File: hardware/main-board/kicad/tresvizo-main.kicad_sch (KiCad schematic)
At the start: 0 parts

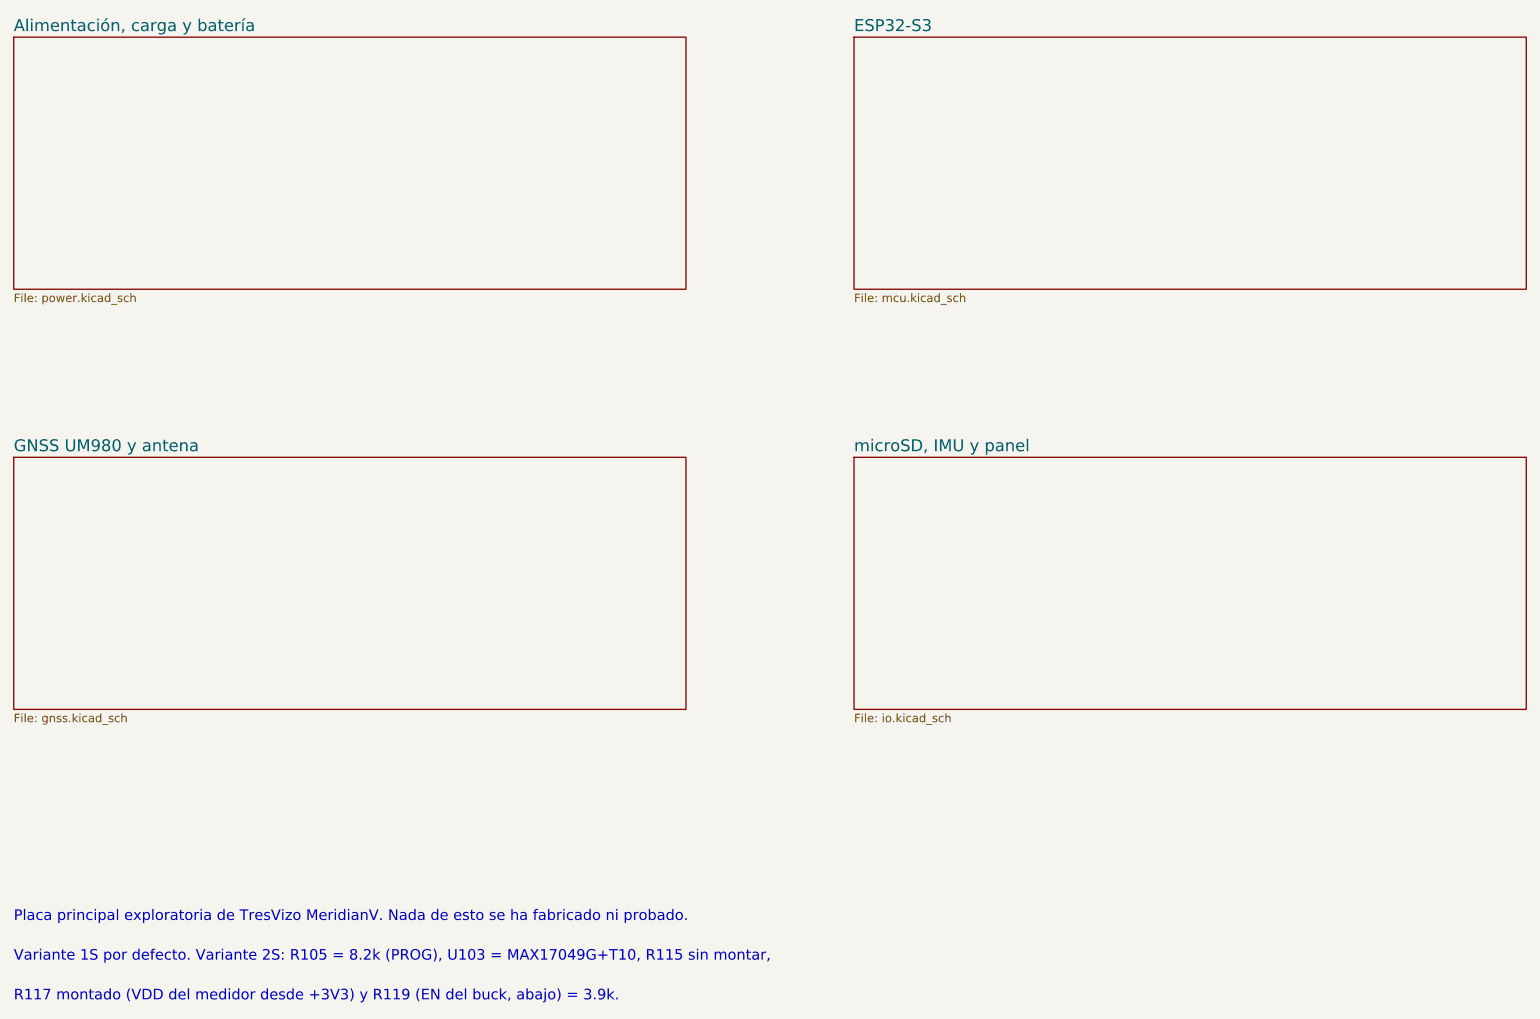
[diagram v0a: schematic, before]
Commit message: Placa principal v0.2: UM980 y BMI088 por cable, conectores hacia cantos o zonas libres, placa panel-usb y un solo panel para JLCPCB
- 46 x 64 mm, 4 capas. El UM980 queda en su carrier BDLX por J301 (GH 8) con 5 V conmutable
  (TPS63070, GPIO45) y el BMI088 vuelve a la tapa por I2C en un segundo bus (J405, GH 7).
- Todos los conectores de cable son GH o SH de 8 pines o menos (kit del propietario), salvo la
  batería (PH 2). Cada uno apunta a un canto o a una zona libre con sitio para la clavija
  enchufada y su cable: áreas de regla clavija_* en el DRC y kicad/plugs.json para el CAD.
- La placa sube 2.5 mm en el tubo (z 23.5-87.5) para que las clavijas del canto inferior tengan
  7.6 mm hasta la base; rieles propuestos en z 39-90 y agujeros nuevos. Comprobada en FreeCAD
  contra V2.2 con modelos 3D y clavijas: sin choques.
- Cargador según el ejemplo de TI: bootstrap junto a sus pines (0.9 y 1.6 mm), salida en abanico
  de la fila inferior y potencia solo por capas externas.
- Placa panel-usb (USB-C a ras de la tapa del panel, GH 8 a J101) y panel de las dos placas con un
  BOM y un CPL (panelize.py, 82.8 x 78 mm).
- Serigrafía sin solapes (silk_clean.py) y logotipo de TresVizo con www.tresvizo.com.
- ERC 0; DRC con 0 errores, 0 avisos, 0 sin conectar y 0 diferencias de paridad en las dos
  placas y el panel. Costo estimado de montaje y piezas: 211 USD por 5 juegos en un panel, sin
  el PCB desnudo.
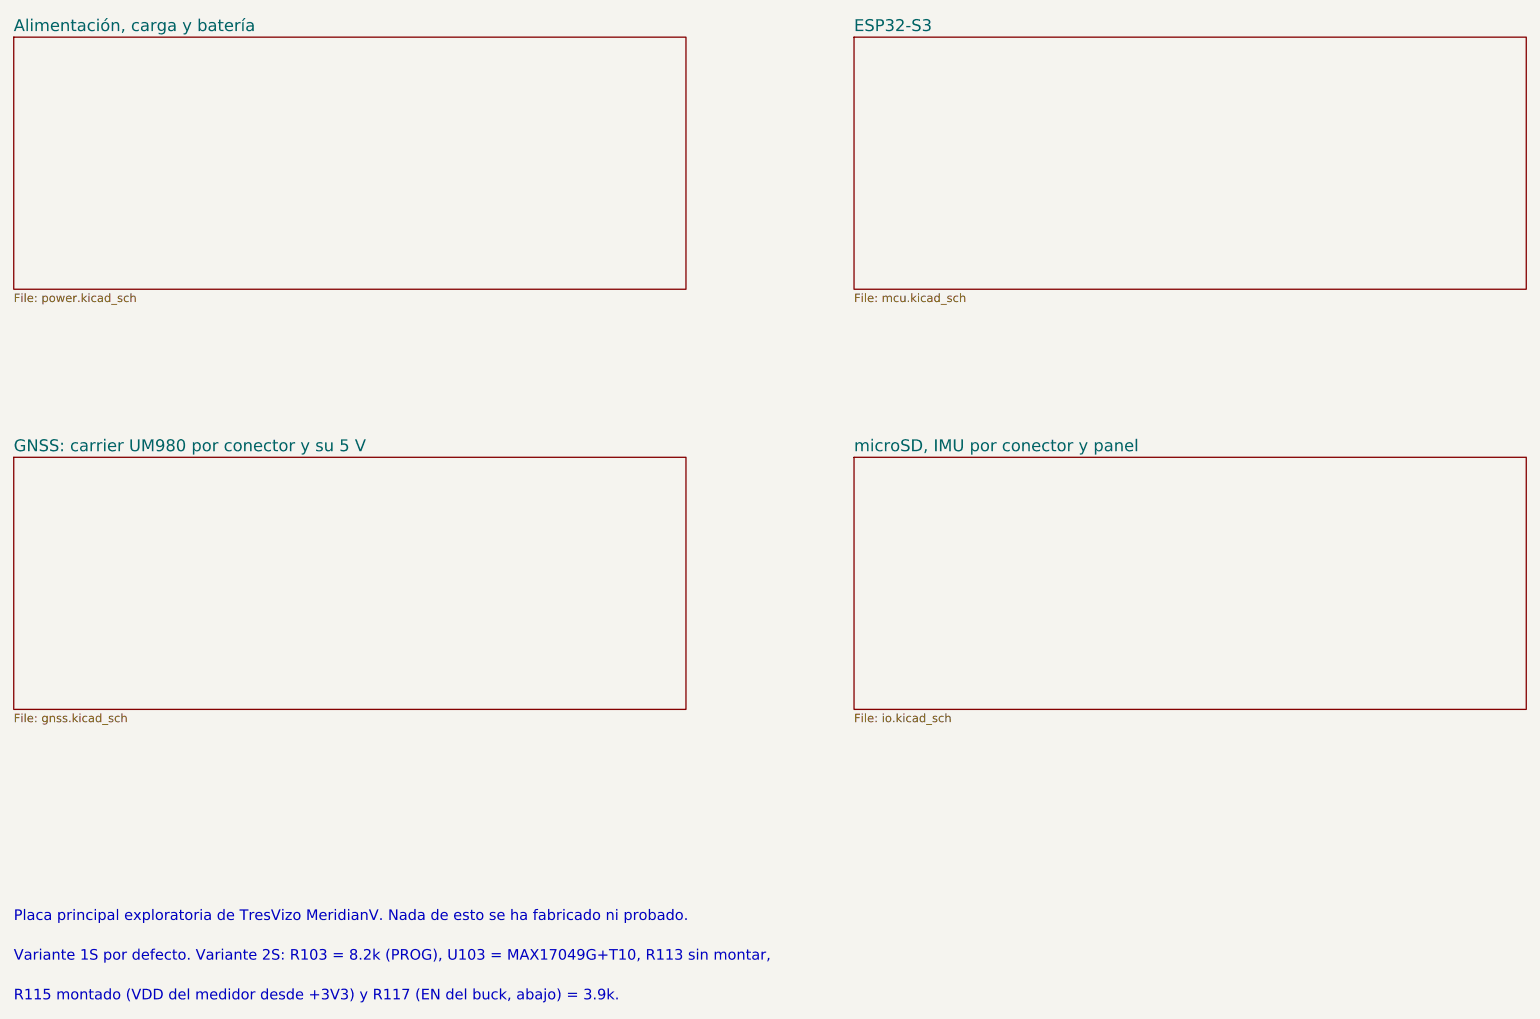
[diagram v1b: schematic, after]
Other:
- sheet GNSS UM980 y antena renamed GNSS: carrier UM980 por conector y su 5 V
- sheet microSD, IMU y panel renamed microSD, IMU por conector y panel
- note added: "R115 montado (VDD del medidor desde +3V3) y R117 (EN del buck, abajo) = 3.9k."
- note added: "Variante 1S por defecto. Variante 2S: R103 = 8.2k (PROG), U103 = MAX17049G+T10, R113 sin montar,"
- note removed: "R117 montado (VDD del medidor desde +3V3) y R119 (EN del buck, abajo) = 3.9k."
- note removed: "Variante 1S por defecto. Variante 2S: R105 = 8.2k (PROG), U103 = MAX17049G+T10, R115 sin montar,"
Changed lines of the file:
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@@
 		(title "TresVizo MeridianV — placa principal")
 		(date "2026-10-04")
-		(rev "0.1")
+		(rev "0.2")
 		(company "TresVizo")
 		(comment 1 "Exploratorio: no fabricado ni probado")
-		(comment 2 "UM980 + ESP32-S3-MINI-1-N4R2 + BMI088 + BQ25798 (1S; 2S por variante)")
-		(comment 3 "JLCPCB 4 capas JLC04161H-7628, 50 x 76 mm")
+		(comment 2 "ESP32-S3-MINI-1-N4R2 + BQ25798 (1S; 2S por variante); GNSS e IMU por conector")
+		(comment 3 "JLCPCB 4 capas JLC04161H-7628")
 	)
 	(sheet
@@
 			(color 0 0 0 0)
 		)
-		(property "Sheetname" "GNSS UM980 y antena"
+		(property "Sheetname" "GNSS: carrier UM980 por conector y su 5 V"
 			(at 30.48 113.6 0)
 			(effects
@@
 			(color 0 0 0 0)
 		)
-		(property "Sheetname" "microSD, IMU y panel"
+		(property "Sheetname" "microSD, IMU por conector y panel"
 			(at 157.48 113.6 0)
 			(effects
@@
 		)
 	)
-	(text "Variante 1S por defecto. Variante 2S: R105 = 8.2k (PROG), U103 = MAX17049G+T10, R115 sin montar,"
+	(text "Variante 1S por defecto. Variante 2S: R103 = 8.2k (PROG), U103 = MAX17049G+T10, R113 sin montar,"
 		(exclude_from_sim no)
 		(at 30.48 188.8 0)
@@
 		)
 	)
-	(text "R117 montado (VDD del medidor desde +3V3) y R119 (EN del buck, abajo) = 3.9k."
+	(text "R115 montado (VDD del medidor desde +3V3) y R117 (EN del buck, abajo) = 3.9k."
 		(exclude_from_sim no)
 		(at 30.48 194.8 0)

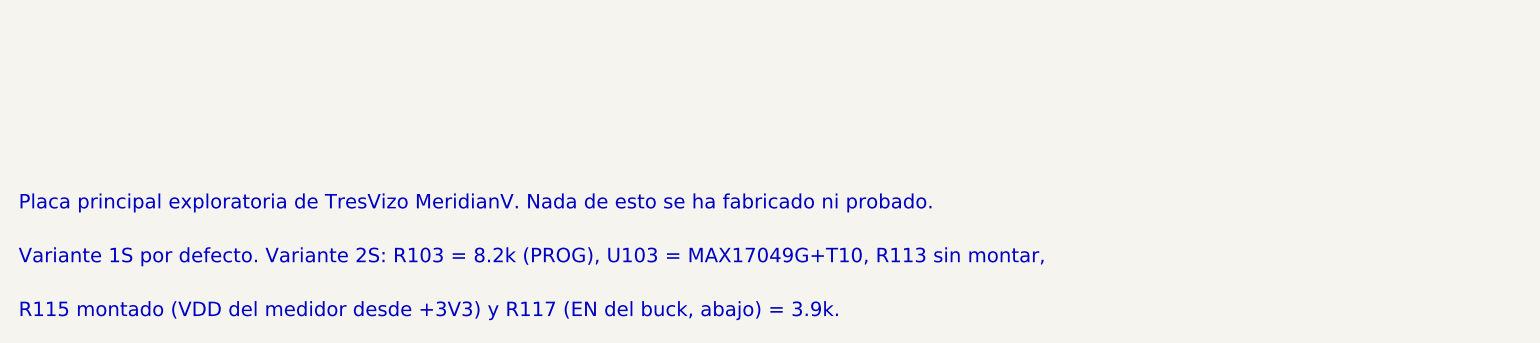
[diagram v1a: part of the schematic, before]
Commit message: Placa principal v0.2: ESP32-S3-WROOM-1-N16R2 en lugar del MINI-1 y sin LEDs del panel
- U201 = ESP32-S3-WROOM-1-N16R2 (C2913205): 16 MB de flash y 2 MB de PSRAM quad. Huella y
  modelos de LCSC; el .step se corrió 3.65 mm para que coincida con su .wrl y la huella.
- GPIO nuevos para rutear el módulo en la misma placa: microSD CLK 6, CMD 7, D0 5, D1 4, D2 16,
  D3 15 y detección 17; UART del GNSS TX 8 / RX 9; PPS 10, EVENT 11, RESET 12; I2C 13/14;
  IMU 41/42 con INT1 2 e INT3 1; botón 18; puntos de prueba en 35, 36 y 37. README y pinout
  con el mapa para el firmware.
- Fuera J406, sus resistencias y la del STAT del cargador: la carcasa V2.3 no lleva LEDs.
- Misma placa de 46 x 64 mm. H1 pasa a (12.0, 9.6) y el corte del riel +X frente a la antena a
  v 15.1-34.0; antena sin cobre en u 0-6.7, v 15.7-33.7.
- R108 sale de debajo de los pines de la microSD (el ruteador se ciclaba entre SD_D3 y
  CHG_INT_N) y el divisor de TS va bajo L102.
- BUCK_SW y el PGND de U105 prerruteados: la vía que el ruteador ponía junto a L102 hacía caer
  el relleno de zonas de KiCad 10 (-11, también en kicad-cli). route_rest guarda las pistas que
  arranca mientras dura el ruteo.
- DRC 0, sin conexiones pendientes y con paridad en la placa y en el panel; ERC 0. Costo
  estimado 206.86 USD por 5 juegos (montaje + piezas, sin PCB).
- Carcasa V2.3: H1 en z 77.9, riel +X cortado en z 53.7-72.4, placa superior recortada frente
  a la antena y SMA de la carrier con las medidas de la foto. Placa nueva contra la carcasa:
  0 mm3 de choques.
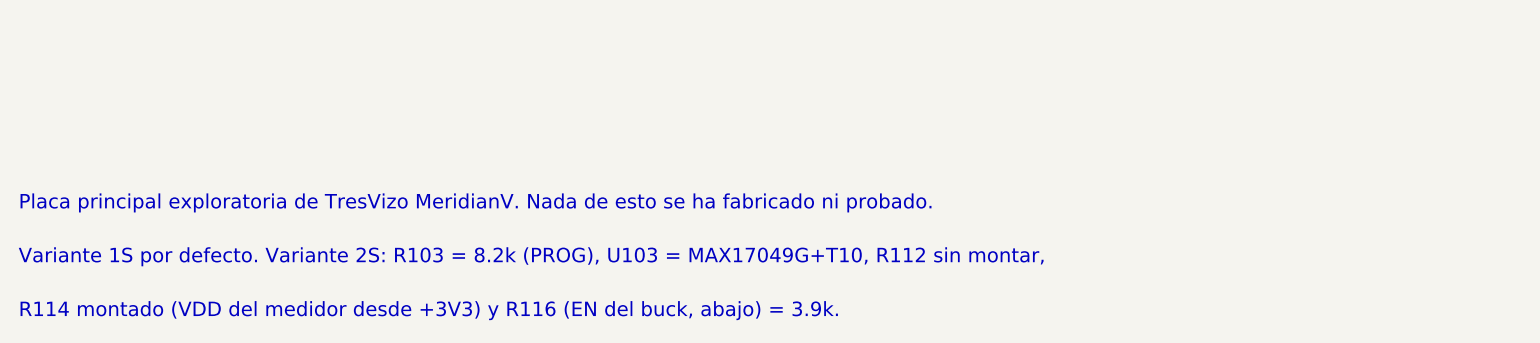
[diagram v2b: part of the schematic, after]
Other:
- note added: "R114 montado (VDD del medidor desde +3V3) y R116 (EN del buck, abajo) = 3.9k."
- note added: "Variante 1S por defecto. Variante 2S: R103 = 8.2k (PROG), U103 = MAX17049G+T10, R112 sin montar,"
- note removed: "R115 montado (VDD del medidor desde +3V3) y R117 (EN del buck, abajo) = 3.9k."
- note removed: "Variante 1S por defecto. Variante 2S: R103 = 8.2k (PROG), U103 = MAX17049G+T10, R113 sin montar,"
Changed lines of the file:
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@@
 		(company "TresVizo")
 		(comment 1 "Exploratorio: no fabricado ni probado")
-		(comment 2 "ESP32-S3-MINI-1-N4R2 + BQ25798 (1S; 2S por variante); GNSS e IMU por conector")
+		(comment 2 "ESP32-S3-WROOM-1-N16R2 + BQ25798 (1S; 2S por variante); GNSS e IMU por conector")
 		(comment 3 "JLCPCB 4 capas JLC04161H-7628")
 	)
@@
 		)
 	)
-	(text "Variante 1S por defecto. Variante 2S: R103 = 8.2k (PROG), U103 = MAX17049G+T10, R113 sin montar,"
+	(text "Variante 1S por defecto. Variante 2S: R103 = 8.2k (PROG), U103 = MAX17049G+T10, R112 sin montar,"
 		(exclude_from_sim no)
 		(at 30.48 188.8 0)
@@
 		)
 	)
-	(text "R115 montado (VDD del medidor desde +3V3) y R117 (EN del buck, abajo) = 3.9k."
+	(text "R114 montado (VDD del medidor desde +3V3) y R116 (EN del buck, abajo) = 3.9k."
 		(exclude_from_sim no)
 		(at 30.48 194.8 0)

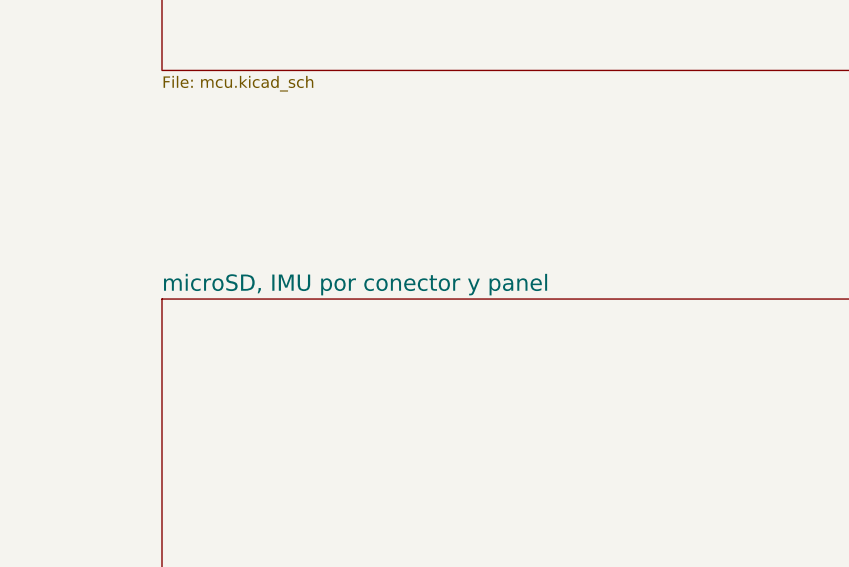
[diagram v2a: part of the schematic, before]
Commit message: Placa principal v0.3 compacta: 36 × 71.5 mm para el tubo de Ø52, con USB-C, OLED, botón, LED y BMI088 en la placa
- Rama exploratoria pedida por el propietario el 07-10-2026. Especificación, interfaces con la
  carcasa, colocación y auditoría en research/v03-compacta.md.
- Esquema (ERC 0):
  - USB-C TYPE-C-31-M-12 con Rd de 5.1k, TVS SMF15A y USBLC6;
  - pulsador TS-1187A a BTN_N;
  - LED de estado en GPIO48 con 330 Ω;
  - OLED del propietario soldada sobre pads SMD (J403);
  - BMI088 por I2C (GPIO41/42, INT1 en GPIO2 e INT3 en GPIO1);
  - J102 en GH 4, con dos contactos por polo;
  - TP208 y TP209 en la UART0.
  Fuera J402, J405 y Q402; la panel-usb ya no se usa.
- Placa de 4 capas con muescas para la funda del USB-C y para la clavija SMA de la carrier.
  - Los bloques del cargador y de los reguladores se mueven sin cambiar su geometría interna.
  - La antena del WROOM va hacia −X, con zona sin cobre.
  - Panel de una sola placa.
  - DRC con 0 violaciones, 0 sin conectar y 0 de paridad; el panel, igual.
- Auditoría eléctrica independiente (08-10-2026), con sus siete puntos corregidos:
  - las soldaduras de la OLED ya no quedan frente al SMA de la carrier;
  - puentes del panel lejos del IMU y de los condensadores de potencia;
  - zona sin cobre de la antena más grande;
  - GND de J102 y vías dobles en VPACK;
  - vías junto al pad de tierra del WROOM;
  - LED más brillante;
  - pads de la UART.
- cad/export_board_step.py exporta el STEP en los ejes de la carcasa, con los modelos de LCSC
  corregidos. cad/check_heights.py comprueba los altos contra el tubo: todas las piezas caben con
  0.3 mm de aire.
- Cambios en los scripts:
  - route_rest.py admite límites de búsqueda por entorno;
  - fanout.py respeta las vías prerruteadas;
  - finish_pcb.py --final quita las vías sin uso;
  - cost_jlc.py sirve para una sola placa.
- Costo estimado en JLCPCB: 236.43 USD por 5 placas montadas, sin el PCB ni el envío.
- El build casi siempre se repite igual. En una de cuatro corrid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
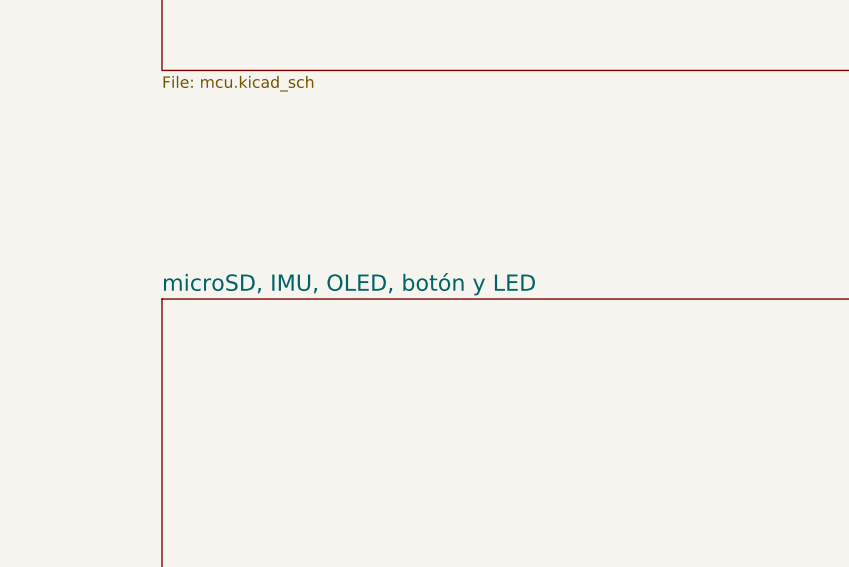
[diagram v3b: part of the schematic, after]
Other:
- sheet microSD, IMU por conector y panel renamed microSD, IMU, OLED, botón y LED
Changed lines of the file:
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@@
 	(title_block
 		(title "TresVizo MeridianV — placa principal")
-		(date "2026-10-04")
-		(rev "0.2")
+		(date "2026-10-07")
+		(rev "0.3")
 		(company "TresVizo")
 		(comment 1 "Exploratorio: no fabricado ni probado")
-		(comment 2 "ESP32-S3-WROOM-1-N16R2 + BQ25798 (1S; 2S por variante); GNSS e IMU por conector")
-		(comment 3 "JLCPCB 4 capas JLC04161H-7628")
+		(comment 2 "ESP32-S3-WROOM-1-N16R2 + BQ25798 (1S; 2S por variante); GNSS por conector")
+		(comment 3 "v0.3 compacta: USB-C, OLED, botón, LED y BMI088 en la placa")
+		(comment 4 "JLCPCB 4 capas JLC04161H-7628")
 	)
 	(sheet
@@
 			(color 0 0 0 0)
 		)
-		(property "Sheetname" "microSD, IMU por conector y panel"
+		(property "Sheetname" "microSD, IMU, OLED, botón y LED"
 			(at 157.48 113.6 0)
 			(effects
